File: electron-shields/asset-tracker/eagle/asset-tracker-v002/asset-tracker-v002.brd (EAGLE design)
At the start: 95.2 x 38.1 mm, 27 parts, among them J1 1X2-3.5MM, T1 DMG3415, U1 FGPMMOPA6H, U3 LIS3DHTR, X1 ELECTRON, X2 uFL, X7 SMA-SMD

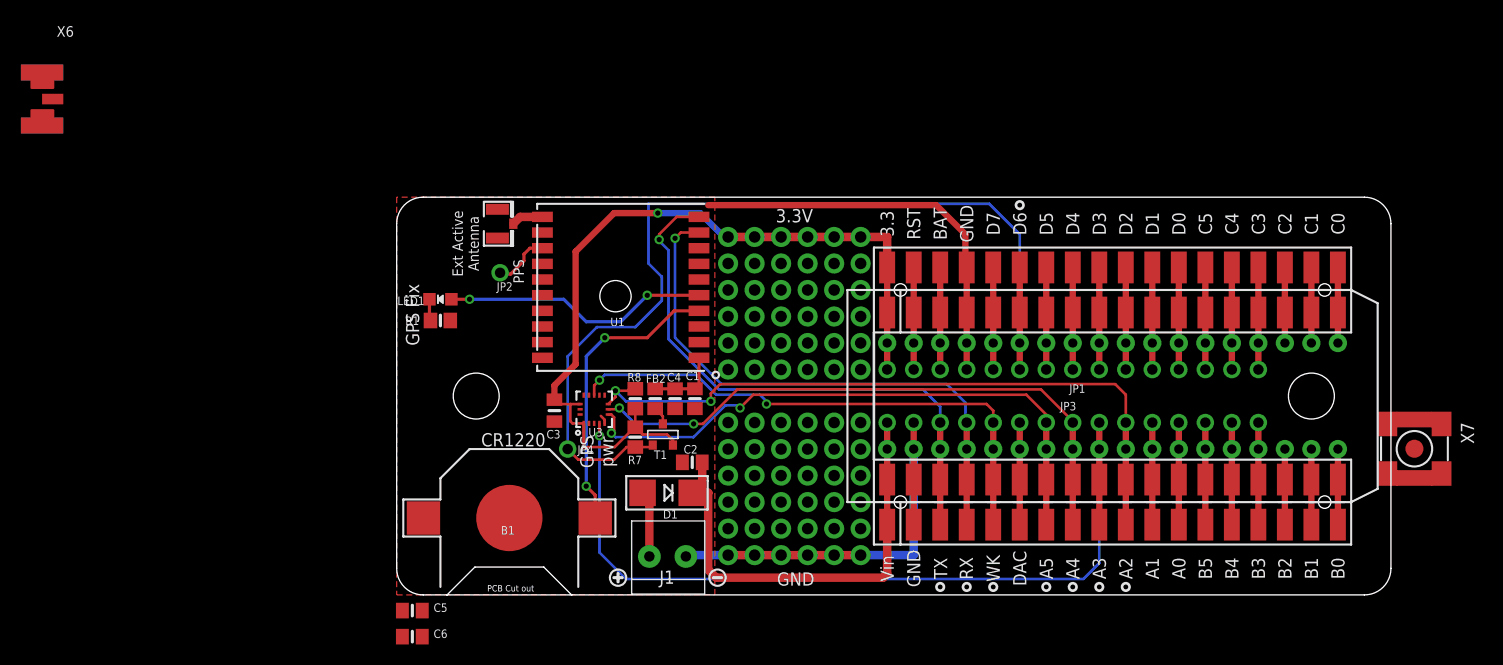
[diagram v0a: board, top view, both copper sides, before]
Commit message: replaced uff with SMA and changed GPS module location
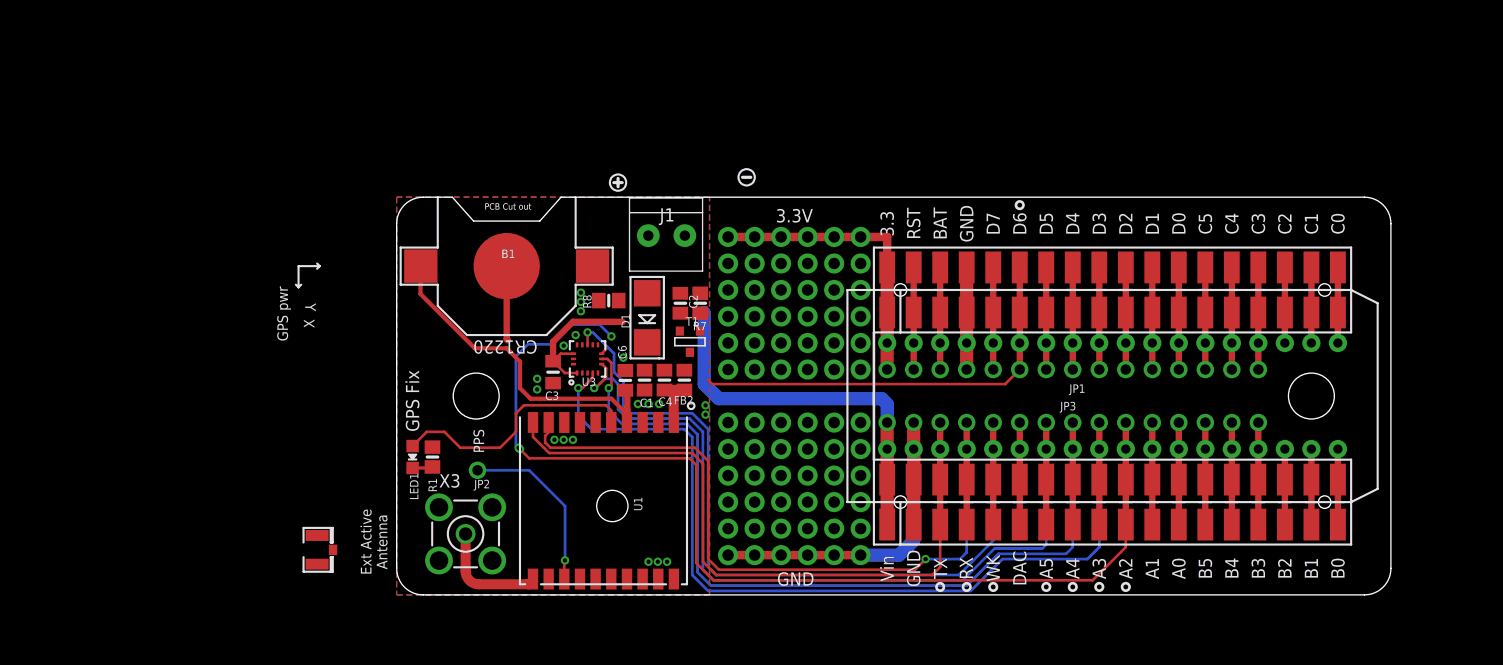
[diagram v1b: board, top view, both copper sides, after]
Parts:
- removed C5: 0.01uF, microbuilder:0805-NO@1
- removed JP4: (no value), microbuilder:1X01_ROUND
- removed X6: (no value), adafruit:SMA_EDGELAUNCH_UFL
- removed X7: SMA-SMD, con-coax:SMA-SMD
- added X3: BU-SMA-V, con-coax:BU-SMA-V
- C1: value 0.1uF -> 0.01uF
- R7: value 10K -> 2K2
- moved U$13 38.5 mm to (33.5, 40.0)
- moved U$21 37.8 mm to (21.2, 39.5)
- moved X2 35.7 mm to (-7.62, 4.32)
- moved C6 31.9 mm to (21.9, 20.6), turned to 90 degrees
- moved J1 30.7 mm to (25.9, 34.4), turned to 180 degrees
- moved B1 24.1 mm to (10.5, 31.5), turned to 0 degrees
- moved U1 20.5 mm to (19.8, 9.02), turned to 270 degrees
- moved JP2 19.0 mm to (7.75, 11.9)
- moved D1 16.9 mm to (24.0, 26.5), turned to 90 degrees
- moved LED1 15.3 mm to (1.52, 13.2), turned to 180 degrees
- moved C2 15.3 mm to (27.2, 27.9), turned to 90 degrees
- moved R7 14.3 mm to (29.1, 27.9)
- moved R1 13.1 mm to (3.43, 13.2), turned to 270 degrees
- moved R8 9.74 mm to (20.3, 28.2), turned to 0 degrees
- moved T1 9.25 mm to (28.1, 24.3), turned to 0 degrees
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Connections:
- removed net GND1: X6.GND@1
- removed net GND2: X6.GND@2
- removed net GND3: X6.GND@3
- removed net GND4: X6.GND@4
- net D6: no longer JP4.1
- net GND: now also J1.2, X3.2, X3.3, X3.4, X3.5; no longer C5.2, J1.1, X2.1, X2.2
- net N$1: no longer C5.1
- net N$4: now also X3.1; no longer X2.3
- net N$9: now also J1.1; no longer J1.2
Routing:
- net D6: track 96.5 -> 40.9 mm
- net 3.3V: track 80.1 -> 42.3 mm, vias 7 -> 6
- net ACCEL_CS: track 67.0 -> 102.8 mm, vias 2 -> 3
- net ACCEL_MISO: track 57.7 -> 85.8 mm, vias 2 -> 1
- net ACCEL_INT1: track 52.2 -> 79.8 mm, vias 2 -> 1
- net GND: track 81.5 -> 54.0 mm, vias 6 -> 25
- net ACCEL_MOSI: track 57.3 -> 84.2 mm, vias 2 -> 1
- net TX: track 54.2 -> 73.4 mm
- net 1PPS: track 5.51 -> 16.8 mm, vias 0 -> 1
- net RX: track 54.9 -> 65.5 mm, vias 1 -> 0
- net N$8: track 44.5 -> 36.7 mm
- net ACCEL_SCK: track 82.6 -> 90.4 mm
- net N$4: track 3.06 -> 10.7 mm
- net N$9: track 7.35 -> 0.00 mm
- net VBACKUP: track 28.5 -> 32.3 mm, vias 2 -> 0
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- added copper zone on layer 16, net GND
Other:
- outline, holes or cut-outs redrawn
- board text added: "X"
- board text added: "Y"

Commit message: routing routing
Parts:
- moved R7 6.93 mm to (23.0, 24.6), turned to 270 degrees
- moved C2 3.66 mm to (28.4, 24.5), turned to 270 degrees
- moved C4 2.79 mm to (28.4, 20.6)
- moved D1 2.62 mm to (25.3, 28.8), turned to 180 degrees
- moved T1 2.44 mm to (25.7, 24.6), turned to 90 degrees
- moved FB2 1.78 mm to (25.8, 20.6)
- moved R8 1.17 mm to (19.4, 27.4), turned to 90 degrees
- moved J1 0.76 mm to (25.1, 34.4)
- moved C1 0.13 mm to (23.9, 20.6)
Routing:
- net N$1: track 4.45 -> 13.1 mm
- net N$9: track 0.00 -> 5.76 mm
- net N$8: track 36.7 -> 40.4 mm
- net VCC: track 0.00 -> 3.31 mm
- net D6: track 40.9 -> 42.5 mm
- net 3.3V: track 42.3 -> 43.9 mm
- net ACCEL_CS: track 102.8 -> 104.0 mm, vias 3 -> 2
